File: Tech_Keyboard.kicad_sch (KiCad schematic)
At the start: 0 parts

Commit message: JScotto tutorial SCHEMATIC ONLY 3x3 keypad
Simply wired a 3x3 numpad according to the video tutorial. If you work on this, please follow ALL instructions from his video https://www.youtube.com/watch?v=8WXpGTIbxlQ

you need his library of placeholders and the like to work on it.
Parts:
- added D1, D2, D3, D4, D5, D6, D7, D8, D9: ~, symbol ScottoKeebs:Placeholder_Diode
- added S1, S2, S3, S4, S5, S6, S7, S8, S9: ~, symbol ScottoKeebs:Placeholder_Keyswitch
- added U1: Arduino_Pro_Micro, ScottoKeebs_MCU:Arduino_Pro_Micro, symbol ScottoKeebs:MCU_Arduino_Pro_Micro
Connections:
- new net Column 0: D1.1 (K), D1.2 (A), D2.1 (K), D2.2 (A), D3.1 (K), D3.2 (A), D4.1 (K), D4.2 (A), D5.1 (K), D5.2 (A), D6.1 (K), D6.2 (A), D7.1 (K), D7.2 (A), D8.1 (K), D8.2 (A), D9.1 (K), D9.2 (A), S1.1, S1.2, S2.1, S2.2, S3.1, S3.2, S4.1, S4.2, S5.1, S5.2, S6.1, S6.2, S7.1, S7.2, S8.1, S8.2, S9.1, S9.2, U1.10 (7/PE6), U1.5 (2/PD1), U1.6 (3/PD0), U1.7 (4/PD4), U1.8 (5/PC6), U1.9 (6/PD7)

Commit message: Update Tech_Keyboard.kicad_sch
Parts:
- added D10, D11, D12, D13, D14, D15: ~, symbol ScottoKeebs:Placeholder_Diode
- added S10, S11, S12, S13, S14, S15: ~, symbol ScottoKeebs:Placeholder_Keyswitch
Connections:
- net Column 0: now also U1.11 (8/PB4), U1.12 (9/PB5), D10.1 (K), D10.2 (A), D11.1 (K), D11.2 (A), D12.1 (K), D12.2 (A), D13.1 (K), D13.2 (A), D14.1 (K), D14.2 (A), D15.1 (K), D15.2 (A), S10.1, S10.2, S11.1, S11.2, S12.1, S12.2, S13.1, S13.2, S14.1, S14.2, S15.1, S15.2

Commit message: Update Tech_Keyboard.kicad_sch
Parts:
- added D16, D17, D18, D19, D20: ~, symbol ScottoKeebs:Placeholder_Diode
- added S16, S17, S18, S19, S20: ~, symbol ScottoKeebs:Placeholder_Keyswitch
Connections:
- net Column 0: now also D16.1 (K), D16.2 (A), D17.1 (K), D17.2 (A), D18.1 (K), D18.2 (A), D19.1 (K), D19.2 (A), D20.1 (K), D20.2 (A), S16.1, S16.2, S17.1, S17.2, S18.1, S18.2, S19.1, S19.2, S20.1, S20.2

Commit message: Update Tech_Keyboard.kicad_sch
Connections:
- net Column 0: now also U1.13 (10/PB6)
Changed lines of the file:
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@@
+	(wire
+		(pts
+			(xy 123.19 83.82) (xy 123.19 74.93)
+		)
+		(stroke
+			(width 0)
+			(type default)
+		)
+	)
 	(wire
 		(pts
@@
 	(global_label "Row 1"
 		(shape input)
+		(at 43.18 99.06 180)
+		(fields_autoplaced yes)
+		(effects
+			(font
+				(size 1.27 1.27)
+			)
+			(justify right)
+		)
+		(property "Intersheetrefs" "${INTERSHEET_REFS}"
+			(at 34.2682 99.06 0)
+			(effects
+				(font
+					(size 1.27 1.27)
+				)
+				(justify right)
+				(hide yes)
+			)
+		)
+	)
+	(global_label "Column 0"
+		(shape input)
+		(at 100.33 74.93 90)
+		(fields_autoplaced yes)
+		(effects
+			(font
+				(size 1.27 1.27)
+			)
+			(justify left)
+		)
+		(property "Intersheetrefs" "${INTERSHEET_REFS}"
+			(at 100.33 62.6922 90)
+			(effects
+				(font
+					(size 1.27 1.27)
+				)
+				(justify left)
+				(hide yes)
+			)
+		)
+	)
+	(global_label "Row 4"
+		(shape input)
+		(at 73.66 104.14 0)
+		(fields_autoplaced yes)
+		(effects
+			(font
+				(size 1.27 1.27)
+			)
+			(justify left)
+		)
+		(property "Intersheetrefs" "${INTERSHEET_REFS}"
+			(at 82.5718 104.14 0)
+			(effects
+				(font
+					(size 1.27 1.27)
+				)
+				(justify left)
+				(hide yes)
+			)
+		)
+	)
+	(global_label "Row 0"
+		(shape input)
 		(at 43.18 96.52 180)
 		(fields_autoplaced yes)
@@
 		)
 	)
-	(global_label "Column 0"
-		(shape input)
-		(at 100.33 74.93 90)
-		(fields_autoplaced yes)
-		(effects
-			(font
-				(size 1.27 1.27)
-			)
-			(justify left)
-		)
-		(property "Intersheetrefs" "${INTERSHEET_REFS}"
-			(at 100.33 62.6922 90)
-			(effects
-				(font
-					(size 1.27 1.27)
-				)
-				(justify left)
-				(hide yes)
-			)
-		)
-	)
-	(global_label "Row 0"
+	(global_label "Row 2"
+		(shape input)
+		(at 43.18 101.6 180)
+		(fields_autoplaced yes)
+		(effects
+			(font
+				(size 1.27 1.27)
+			)
+			(justify right)
+		)
+		(property "Intersheetrefs" "${INTERSHEET_REFS}"
+			(at 34.2682 101.6 0)
+			(effects
+				(font
+					(size 1.27 1.27)
+				)
+				(justify right)
+				(hide yes)
+			)
+		)
+	)
+	(global_label "Row 3"
+		(shape input)
+		(at 43.18 104.14 180)
+		(fields_autoplaced yes)
+		(effects
+			(font
+				(size 1.27 1.27)
+			)
+			(justify right)
+		)
+		(property "Intersheetrefs" "${INTERSHEET_REFS}"
+			(at 34.2682 104.14 0)
+			(effects
+				(font
+					(size 1.27 1.27)
+				)
+				(justify right)
+				(hide yes)
+			)
+		)
+	)
+	(global_label "Column 1"
+		(shape input)
+		(at 43.18 88.9 180)
+		(fields_autoplaced yes)
+		(effects
+			(font
+				(size 1.27 1.27)
+			)
+			(justify right)
+		)
+		(property "Intersheetrefs" "${INTERSHEET_REFS}"
+			(at 30.9422 88.9 0)
+			(effects
+				(font
+					(size 1.27 1.27)
+				)
+				(justify right)
+				(hide yes)
+			)
+		)
+	)
+	(global_label "Column 2"
+		(shape input)
+		(at 43.18 91.44 180)
+		(fields_autoplaced yes)
+		(effects
+			(font
+				(size 1.27 1.27)
+			)
+			(justify right)
+		)
+		(property "Intersheetrefs" "${INTERSHEET_REFS}"
+			(at 30.9422 91.44 0)
+			(effects
+				(font
+					(size 1.27 1.27)
+				)
+				(justify right)
+				(hide yes)
+			)
+		)
+	)
+	(global_label "Row 3"
+		(shape input)
+		(at 130.81 130.81 0)
+		(fields_autoplaced yes)
+		(effects
+			(font
+				(size 1.27 1.27)
+			)
+			(justify left)
+		)
+		(property "Intersheetrefs" "${INTERSHEET_REFS}"
+			(at 139.7218 130.81 0)
+			(effects
+				(font
+					(size 1.27 1.27)
+				)
+				(justify left)
+				(hide yes)
+			)
+		)
+	)
+	(global_label "Column 2"
+		(shape input)
+		(at 115.57 74.93 90)
+		(fields_autoplaced yes)
+		(effects
+			(font
+				(size 1.27 1.27)
+			)
+			(justify left)
+		)
+		(property "Intersheetrefs" "${INTERSHEET_REFS}"
+			(at 115.57 62.6922 90)
+			(effects
+				(font
+					(size 1.27 1.27)
+				)
+				(justify left)
+				(hide yes)
+			)
+		)
+	)
+	(global_label "Column 3"
 		(shape input)
 		(at 43.18 93.98 180)
@@
 		)
 		(property "Intersheetrefs" "${INTERSHEET_REFS}"
-			(at 34.2682 93.98 0)
-			(effects
-				(font
-					(size 1.27 1.27)
-				)
-				(justify right)
-				(hide yes)
-			)
-		)
-	)
-	(global_label "Row 2"
-		(shape input)
-		(at 43.18 99.06 180)
-		(fields_autoplaced yes)
-		(effects
-			(font
-				(size 1.27 1.27)
-			)
-			(justify right)
-		)
-		(property "Intersheetrefs" "${INTERSHEET_REFS}"
-			(at 34.2682 99.06 0)
-			(effects
-				(font
-					(size 1.27 1.27)
-				)
-				(justify right)
-				(hide yes)
-			)
-		)
-	)
-	(global_label "Row 3"
-		(shape input)
-		(at 43.18 101.6 180)
-		(fields_autoplaced yes)
-		(effects
-			(font
-				(size 1.27 1.27)
-			)
-			(justify right)
-		)
-		(property "Intersheetrefs" "${INTERSHEET_REFS}"
-			(at 34.2682 101.6 0)
-			(effects
-				(font
-					(size 1.27 1.27)
-				)
-				(justify right)
-				(hide yes)
-			)
-		)
-	)
-	(global_label "Column 1"
-		(shape input)
-		(at 43.18 88.9 180)
-		(fields_autoplaced yes)
-		(effects
-			(font
-				(size 1.27 1.27)
-			)
-			(justify right)
-		)
-		(property "Intersheetrefs" "${INTERSHEET_REFS}"
-			(at 30.9422 88.9 0)
-			(effects
-				(font
-					(size 1.27 1.27)
-				)
-				(justify right)
-				(hide yes)
-			)
-		)
-	)
-	(global_label "Column 2"
-		(shape input)
-		(at 43.18 91.44 180)
-		(fields_autoplaced yes)
-		(effects
-			(font
-				(size 1.27 1.27)
-			)
-			(justify right)
-		)
-		(property "Intersheetrefs" "${INTERSHEET_REFS}"
-			(at 30.9422 91.44 0)
-			(effects
-				(font
-					(size 1.27 1.27)
-				)
-				(justify right)
-				(hide yes)
-			)
-		)
-	)
-	(global_label "Row 4"
-		(shape input)
-		(at 43.18 104.14 180)
-		(fields_autoplaced yes)
-		(effects
-			(font
-				(size 1.27 1.27)
-			)
-			(justify right)
-		)
-		(property "Intersheetrefs" "${INTERSHEET_REFS}"
-			(at 34.2682 104.14 0)
-			(effects
-				(font
-					(size 1.27 1.27)
-				)
-				(justify right)
-				(hide yes)
-			)
-		)
-	)
-	(global_label "Row 3"
-		(shape input)
-		(at 130.81 130.81 0)
-		(fields_autoplaced yes)
-		(effects
-			(font
-				(size 1.27 1.27)
-			)
-			(justify left)
-		)
-		(property "Intersheetrefs" "${INTERSHEET_REFS}"
-			(at 139.7218 130.81 0)
-			(effects
-				(font
-					(size 1.27 1.27)
-				)
-				(justify left)
-				(hide yes)
-			)
-		)
-	)
-	(global_label "Column 2"
-		(shape input)
-		(at 115.57 74.93 90)
-		(fields_autoplaced yes)
-		(effects
-			(font
-				(size 1.27 1.27)
-			)
-			(justify left)
-		)
-		(property "Intersheetrefs" "${INTERSHEET_REFS}"
-			(at 115.57 62.6922 90)
-			(effects
-				(font
+			(at 30.9422 93.98 0)
+			(effects
+				(font
+					(size 1.27 1.27)
+				)
+				(justify right)
+				(hide yes)
+			)
+		)
+	)
+	(global_label "Column 3"
+		(shape input)
+		(at 123.19 74.93 90)
+		(fields_autoplaced yes)
+		(effects
+			(font
+				(size 1.27 1.27)
+			)
+			(justify left)
+		)
+		(property "Intersheetrefs" "${INTERSHEET_REFS}"
+			(at 123.19 62.6922 90)
+			(effects
+				(font

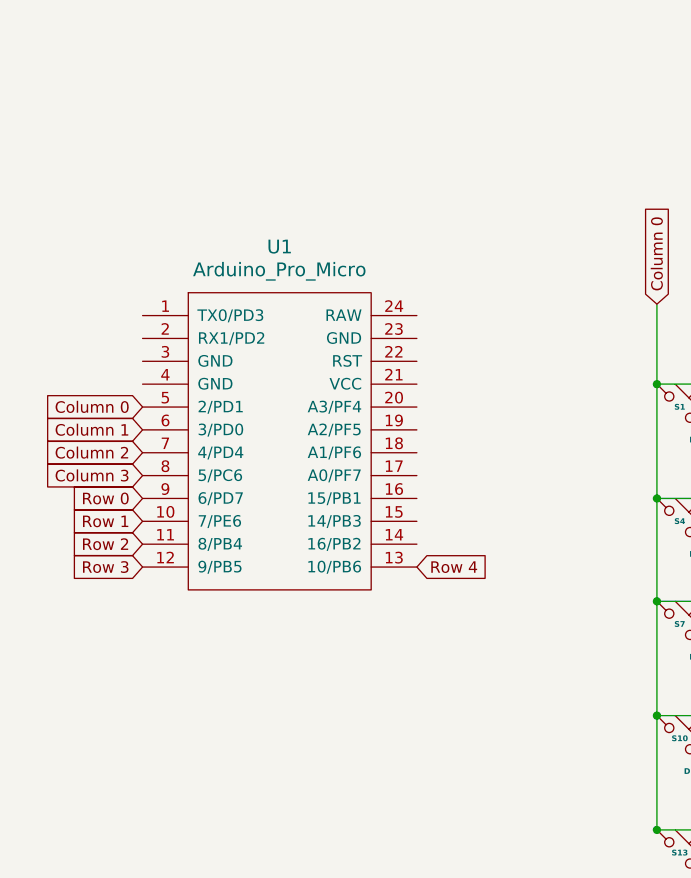
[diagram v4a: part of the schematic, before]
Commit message: changed to generic pro micro, unwired rotary encoder
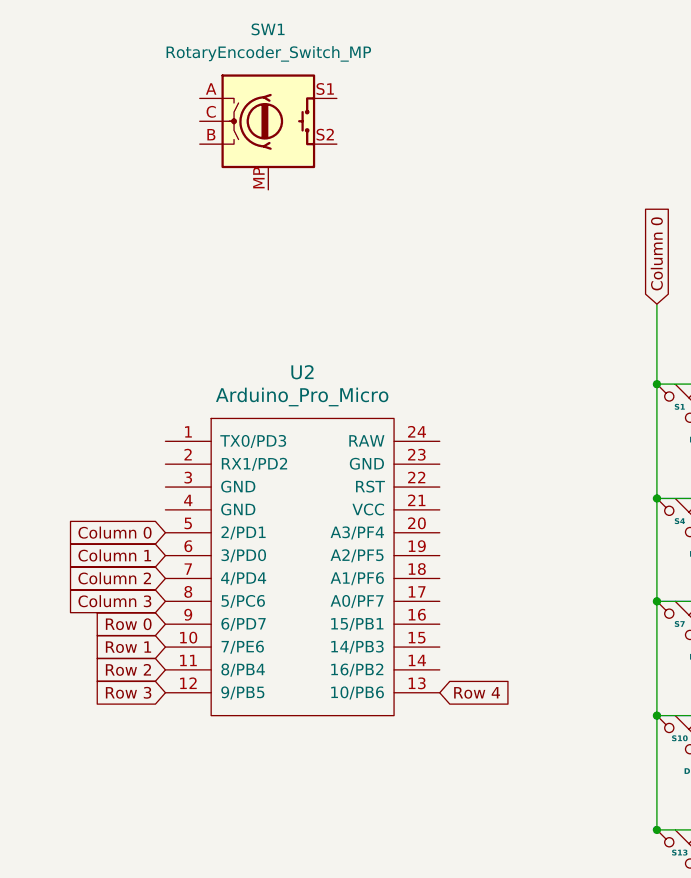
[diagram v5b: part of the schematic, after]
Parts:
- removed U1: Arduino_Pro_Micro, ScottoKeebs_MCU:Arduino_Pro_Micro, symbol ScottoKeebs:MCU_Arduino_Pro_Micro
- added SW1: RotaryEncoder_Switch_MP, symbol Device:RotaryEncoder_Switch_MP
- added U2: Arduino_Pro_Micro, ScottoKeebs_MCU:Arduino_Pro_Micro, symbol ScottoKeebs:MCU_Arduino_Pro_Micro
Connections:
- net Column 0: now also U2.10 (7/PE6), U2.11 (8/PB4), U2.12 (9/PB5), U2.13 (10/PB6), U2.5 (2/PD1), U2.6 (3/PD0), U2.7 (4/PD4), U2.8 (5/PC6), U2.9 (6/PD7)

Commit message: Update Tech_Keyboard.kicad_sch
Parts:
- removed S1: ~, symbol ScottoKeebs:Placeholder_Keyswitch
- removed U2: Arduino_Pro_Micro, ScottoKeebs_MCU:Arduino_Pro_Micro, symbol ScottoKeebs:MCU_Arduino_Pro_Micro
- added U1: MCU_Seeed_XIAO_RP2040, symbol ScottoKeebs:MCU_Seeed_XIAO_RP2040
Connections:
- net Column 0: now also SW1.S1, U1.1 (PA02_A0_D0), U1.10 (PA5_A9_D9_MISO), U1.11 (PA6_A10_D10_MOSI), U1.2 (PA4_A1_D1), U1.3 (PA10_A2_D2), U1.4 (PA11_A3_D3), U1.5 (PA8_A4_D4_SDA), U1.6 (PA9_A5_D5_SCL), U1.7 (PB08_A6_D6_TX)
- net at SW1.A: now also U1.9 (PA7_A8_D8_SCK)
- net at SW1.B: now also U1.8 (PB09_A7_D7_RX)
- net at SW1.C: now also U1.13 (GND)
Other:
- moved on the sheet: SW1

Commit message: Update Tech_Keyboard.kicad_sch
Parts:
- renumbered S2 to S1, S9 to S10, S18 to S11, S10 to S12, S11 to S13, S12 to S14, S19 to S15, S13 to S16, S14 to S17, S15 to S18, S20 to S19, S3 to S2, S16 to S3, S17 to S7, S7 to S8, S8 to S9
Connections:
- net at SW1.C, U1.13 (GND): now also SW1.S2
- net R1: now reaches SW1.B, U1.8 (PB09_A7_D7_RX)
- net R0: now reaches SW1.A, U1.9 (PA7_A8_D8_SCK)

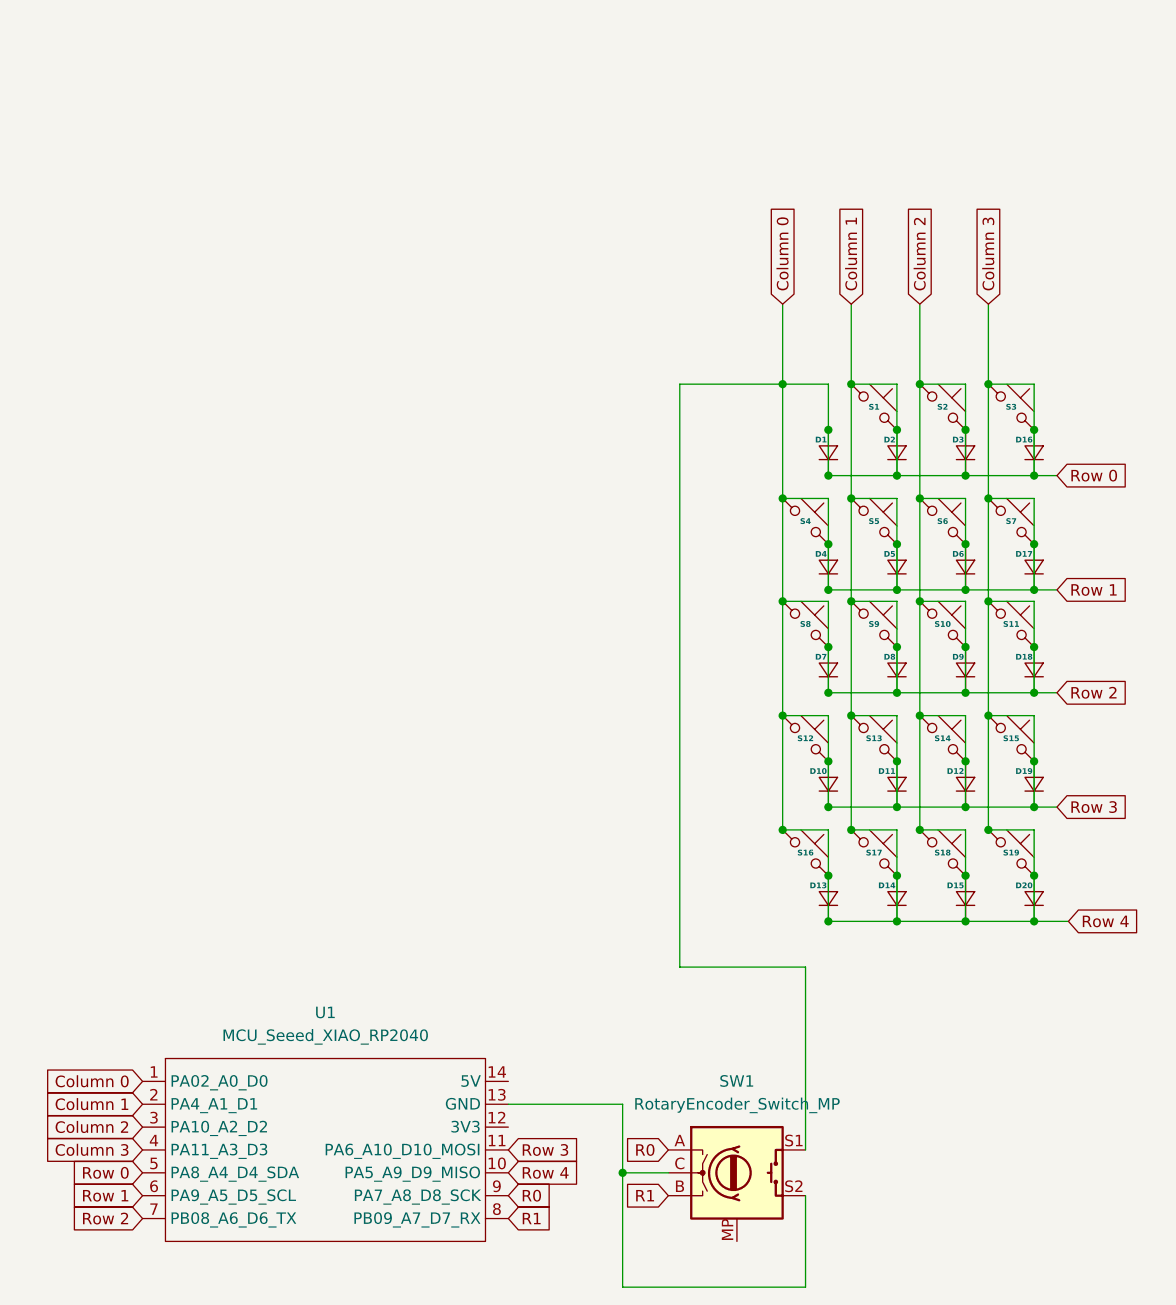
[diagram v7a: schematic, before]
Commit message: New numpad layout and schematic and pcb
schematic and pcb fixed mostly. No wiring done yet on pcb again. Removed the push button the on the rotary encoder for simplicity due to overloading pin count.
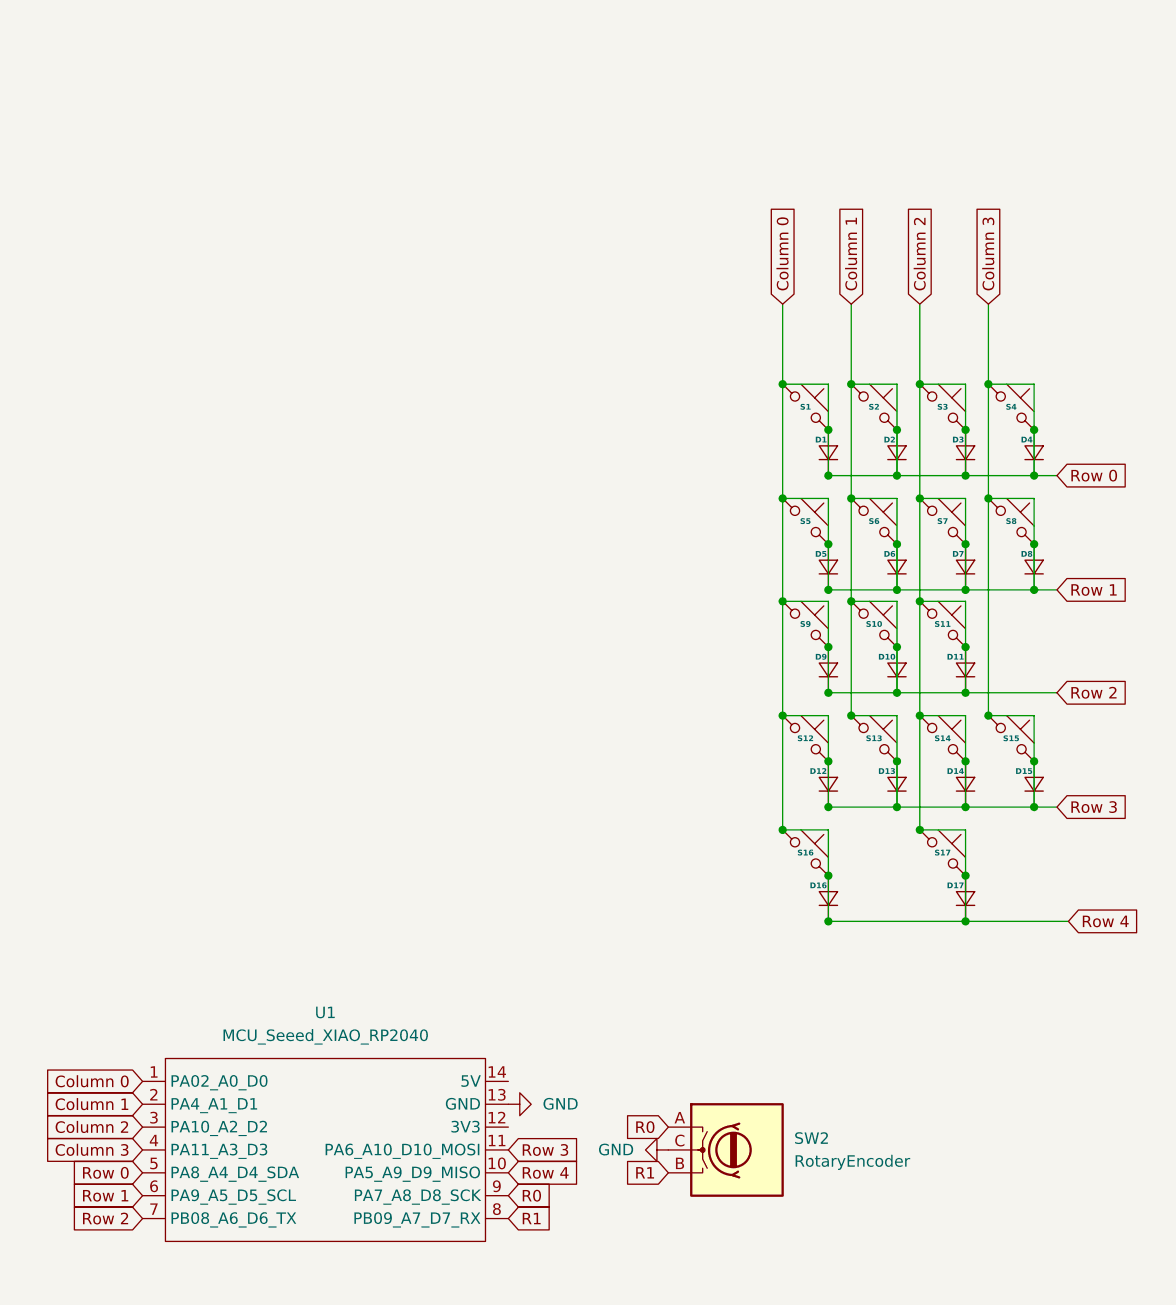
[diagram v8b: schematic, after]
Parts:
- removed D14, D18, D20: ~, symbol ScottoKeebs:Placeholder_Diode
- removed S11, S17, S19: ~, symbol ScottoKeebs:Placeholder_Keyswitch
- removed SW1: RotaryEncoder_Switch_MP, symbol Device:RotaryEncoder_Switch_MP
- added S1: ~, symbol ScottoKeebs:Placeholder_Keyswitch
- added SW2: RotaryEncoder, symbol Device:RotaryEncoder
- renumbered D8 to D10, D9 to D11, D10 to D12, D11 to D13, D12 to D14, D19 to D15, D13 to D16, D15 to D17, D16 to D4, D4 to D5, D5 to D6, D6 to D7, D17 to D8, D7 to D9, S9 to S10, S10 to S11, S18 to S17, S1 to S2, S2 to S3, S3 to S4, S4 to S5, S5 to S6, S6 to S7, S7 to S8, S8 to S9
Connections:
- net Column 0: now also S1.1, S1.2
- net R0: now also SW2.A
- net R1: now also SW2.B
- net GND: now reaches U1.13 (GND)
- net GND: now also SW2.C
